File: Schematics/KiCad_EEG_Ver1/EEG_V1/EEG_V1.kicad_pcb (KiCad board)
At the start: 2 copper layers, 82 parts, among them U1 INA819IDGK, U10 OPA172IDR, U11 OPA172IDR, U12 OPA172IDR, U13 OPA172IDR, U4 OPA172IDR, U5 OPA172IDR, U6 OPA172IDR, U7 OPA172IDR, U8 OPA172IDR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

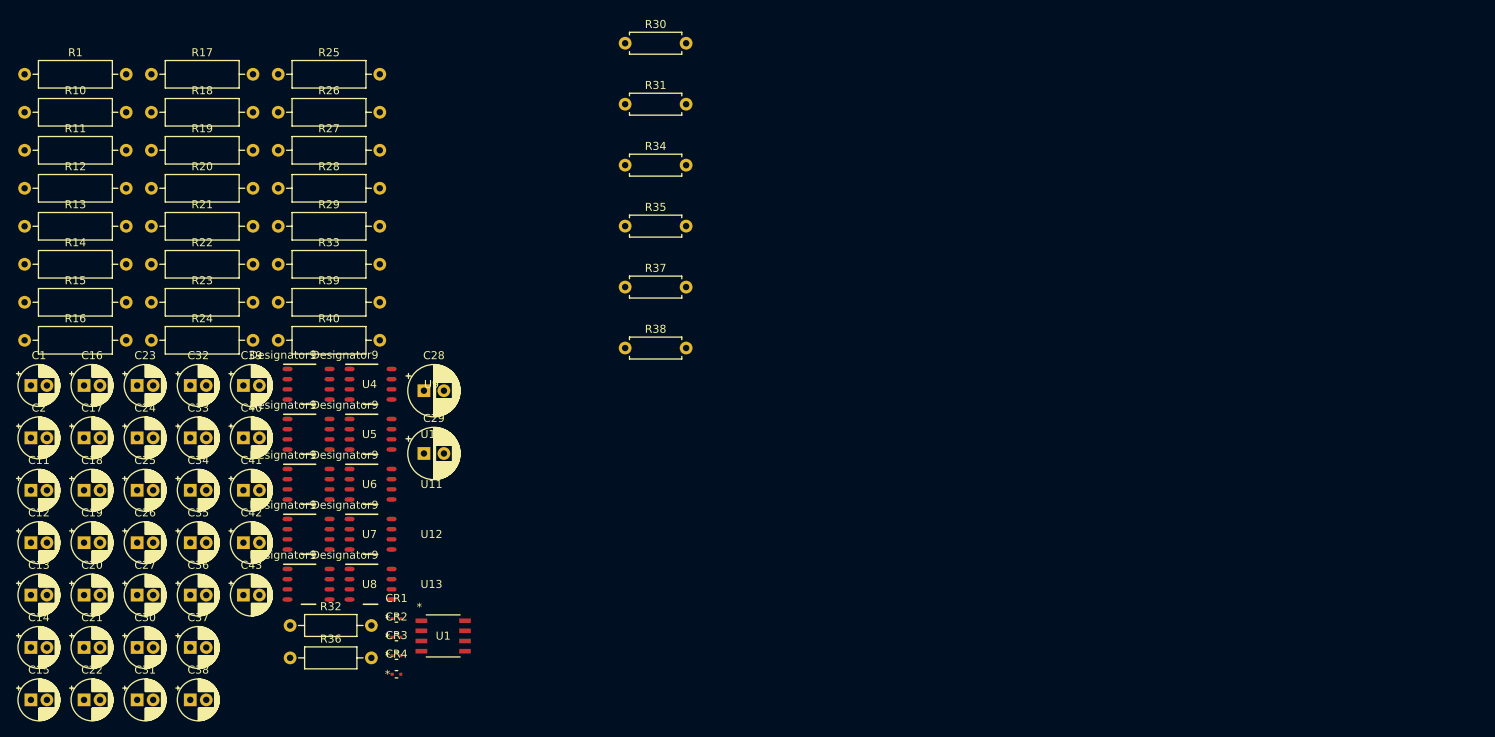
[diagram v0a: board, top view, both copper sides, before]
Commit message: Twin rejection filter modeled
This is a prelim layout but i definitely reckon i can squeeze the rectangular config of the two stages into more of a square config.
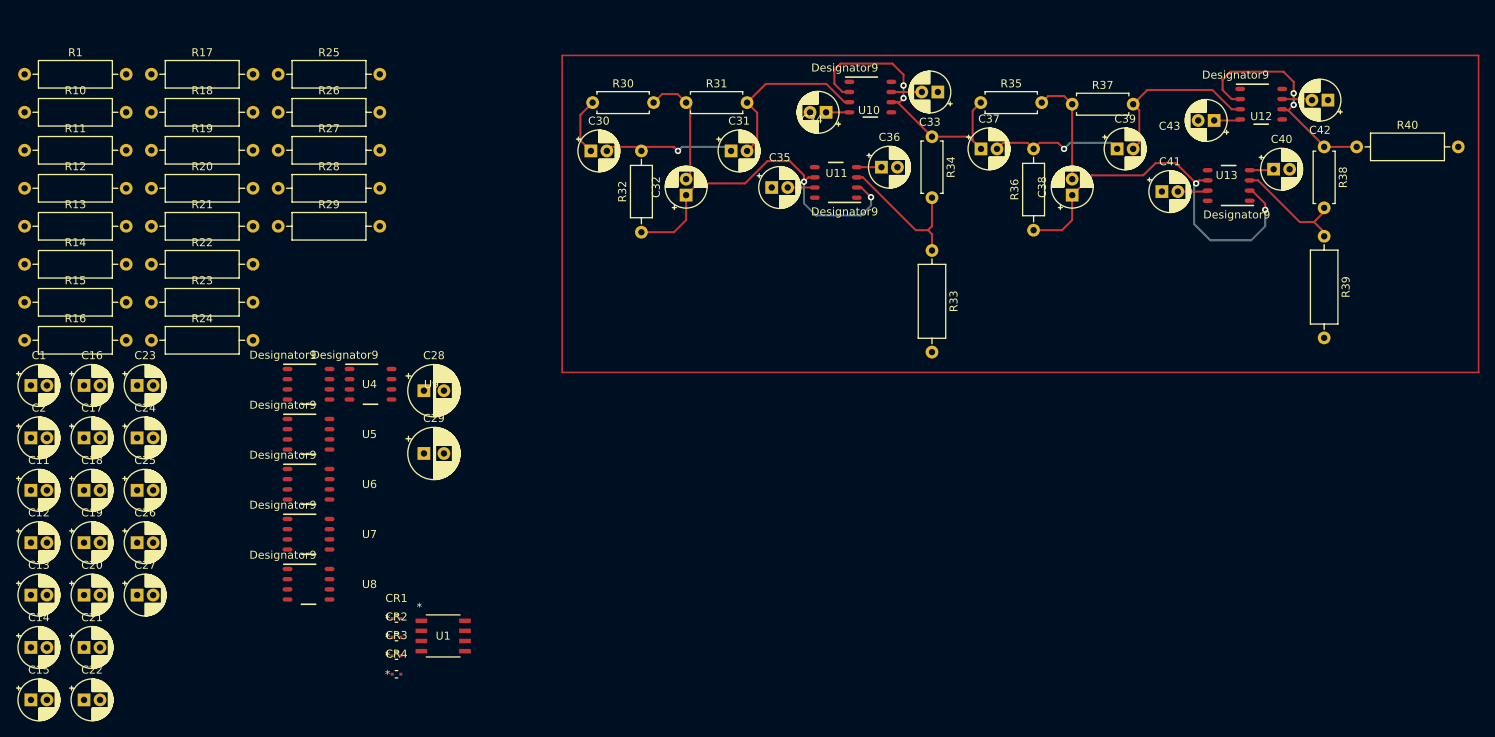
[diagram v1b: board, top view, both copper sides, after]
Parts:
- moved C42 146.4 mm to (245.3, 45.2), turned to 180 degrees
- moved R40 137.0 mm to (248.9, 51.1)
- moved C43 135.1 mm to (231.1, 47.8), turned to 180 degrees
- moved C40 133.1 mm to (238.5, 53.8)
- moved R39 131.0 mm to (244.9, 62.2), turned to -90 degrees
- moved C38 127.0 mm to (213.4, 57.1), turned to 90 degrees
- moved U12 123.6 mm to (237.0, 45.7)
- moved C41 120.7 mm to (224.6, 56.6)
- moved U13 118.3 mm to (232.9, 55.9), turned to 180 degrees
- moved C37 116.8 mm to (202.0, 51.3)
- moved C39 113.2 mm to (219.0, 51.3)
- moved R36 107.2 mm to (208.5, 61.5), turned to 90 degrees
- moved C33 103.0 mm to (196.6, 44.2), turned to 180 degrees
- moved C36 101.6 mm to (189.5, 53.6)
- moved C31 101.1 mm to (170.7, 51.6)
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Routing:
- net Net-(U13A-IN-): track 0.00 -> 49.3 mm, vias 0 -> 2
- net Net-(U11A-IN-): track 0.00 -> 45.7 mm, vias 0 -> 2
- net Net-(U10A-IN-): track 0.00 -> 37.4 mm, vias 0 -> 2
- net Net-(U12A-IN-): track 0.00 -> 28.9 mm, vias 0 -> 2
- net Net-(U10A-IN+): track 0.00 -> 21.8 mm
- net Net-(U12A-IN+): track 0.00 -> 21.3 mm
- net Net-(U11A-IN+): track 0.00 -> 18.7 mm
- net Net-(C37-Pad2): track 0.00 -> 16.9 mm, vias 0 -> 1
- net Net-(C30-Pad2): track 0.00 -> 16.8 mm, vias 0 -> 1
- net Net-(U13A-IN+): track 0.00 -> 15.6 mm
- net Net-(C32-Pad2): track 0.00 -> 14.9 mm
- net V++: track 0.00 -> 14.0 mm
- net Net-(C38-Pad2): track 0.00 -> 13.9 mm
- net V--: track 0.00 -> 12.3 mm
- net Notch_in: track 0.00 -> 7.21 mm
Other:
- board text added: "Designator9"
- board text added: "Please check this join as Im not sure how correct this is"
- board text added: "Please check this use of {dblquote}via{dblquote} to attach wires to pads"
